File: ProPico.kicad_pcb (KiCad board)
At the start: 2 copper layers, 59 parts, among them J1 USB_C_Receptacle_USB2.0, J2 SWD, J3 LEFT, J4 RIGHT, SW1 BOOTSEL, SW2 RES, U1 FM24CL16B, U2 W25Q128JVS, U3 TLV1117-33, U4 LM4040DBZ-3, U5 RP2040, Y1 ECS-120-12-36-AGN-TR3

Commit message: started layout
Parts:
- removed C19, C20: 100n, Capacitor_SMD:C_0402_1005Metric
- removed FB1: 100 @ 100MHz, Inductor_SMD:L_0805_2012Metric_Pad1.15x1.40mm_HandSolder
- removed REF**: RPi_Pico_SMD_TH, MCU_RaspberryPi_and_Boards:RPi_Pico_SMD_TH
- C1, C5: value 2.2u -> 100n; footprint Capacitor_SMD:C_0603_1608Metric_Pad1.08x0.95mm_HandSolder -> Capacitor_SMD:C_0402_1005Metric_Pad0.74x0.62mm_HandSolder
- C10: value 100n -> 1u
- C14: value 1u -> 100n
- C2: value 100n -> 18p; footprint Capacitor_SMD:C_0402_1005Metric_Pad0.74x0.62mm_HandSolder -> Capacitor_SMD:C_0402_1005Metric
- C4: value 18p -> 2.2u; footprint Capacitor_SMD:C_0402_1005Metric -> Capacitor_SMD:C_0603_1608Metric_Pad1.08x0.95mm_HandSolder
- C6: value 2.2u -> 10u; footprint Capacitor_SMD:C_0603_1608Metric_Pad1.08x0.95mm_HandSolder -> Capacitor_SMD:C_0805_2012Metric_Pad1.18x1.45mm_HandSolder
- C7: value 100n -> 10n C0G; footprint Capacitor_SMD:C_0402_1005Metric_Pad0.74x0.62mm_HandSolder -> Capacitor_SMD:C_0603_1608Metric_Pad1.08x0.95mm_HandSolder
- C8: value 10u -> 100n; footprint Capacitor_SMD:C_0805_2012Metric_Pad1.18x1.45mm_HandSolder -> Capacitor_SMD:C_0402_1005Metric
- C9: value 10n C0G -> 100n; footprint Capacitor_SMD:C_0603_1608Metric_Pad1.08x0.95mm_HandSolder -> Capacitor_SMD:C_0402_1005Metric
- TP1: value GND -> BOOTSEL; moved to B.Cu
- TP2: value D- -> VREG; moved to B.Cu
- TP3: value D+ -> GP25; moved to B.Cu
- TP4: value GP24 -> GND
- TP5: value GP25 -> D+
- TP6: value BOOTSEL -> GP24
- TP7: value VREG -> D-
- moved D1 87.0 mm to (161.4, 54.0), turned to 90 degrees
- moved C4 78.5 mm to (160.4, 57.4), turned to 180 degrees
- moved R7 78.5 mm to (161.4, 89.6), turned to -90 degrees
- moved C11 75.6 mm to (160.5, 75.4)
- moved R10 75.3 mm to (154.1, 85.7)
- moved R5 75.2 mm to (153.2, 81.4), turned to 180 degrees
- moved R11 75.0 mm to (154.1, 86.9)
- moved C12 74.5 mm to (157.7, 68.7), turned to 90 degrees
- moved C6 73.4 mm to (161.7, 65.3), turned to -90 degrees
- moved C1 73.0 mm to (151.4, 86.9), turned to 180 degrees
- moved C14 72.8 mm to (160.5, 70.9)
- moved C10 72.6 mm to (156.7, 68.7), turned to 90 degrees
- moved R9 71.9 mm to (156.1, 66.8), turned to -90 degrees
- moved R8 71.4 mm to (155.1, 66.8), turned to -90 degrees
- moved C9 71.1 mm to (156.0, 80.6), turned to -90 degrees
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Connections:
- C1 pad 1: +5VD -> +3V3
- C11 pad 1: +1V1 -> +3V3
- C12 pad 1: +1V1 -> +3V3
- C2 pad 1: +3V3 -> /XIN
- C3 pad 1: /XIN -> Net-(C3-Pad1)
- C4 pad 1: Net-(C4-Pad1) -> +5V
- C6 pad 1: +5V -> Net-(C6-Pad1)
- C7 pad 1: +3V3 -> /ADC_AVDD
- C8 pad 1: Net-(C8-Pad1) -> +1V1
- C9 pad 1: /ADC_AVDD -> +1V1
- D1 pad 1: +5VD -> +5V
- J1 pad S1: unconnected-(J1-SHIELD-PadS1) -> GND
- R5 pad 2: Net-(C4-Pad1) -> Net-(C3-Pad1)
- R6 pad 1: Net-(C8-Pad1) -> Net-(C6-Pad1)
- TP1 pad 1: GND -> Net-(R1-Pad2)
- TP2 pad 1: /D- -> +1V1
- TP3 pad 1: /D+ -> /EEPROM_SCL
- TP4 pad 1: /EEPROM_SDA -> GND
- TP5 pad 1: /EEPROM_SCL -> /D+
- TP6 pad 1: Net-(R1-Pad2) -> /EEPROM_SDA
- TP7 pad 1: +1V1 -> /D-
- Y1 pad 1: Net-(C4-Pad1) -> Net-(C3-Pad1)
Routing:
- net Net-(J1-CC2): track 0.00 -> 2.67 mm
- net Net-(J1-CC1): track 0.00 -> 2.61 mm
- net Net-(D2-K): track 0.00 -> 1.41 mm
- net GND: vias 0 -> 4
- added copper zone on F.Cu, net +5V
- added copper zone on F.Cu, net GND
- added copper zone on F.Cu, net VBUS
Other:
- board outline added: 21 x 51 mm

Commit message: progress on layout
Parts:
- moved JP1 5.55 mm to (153.6, 95.6), turned to 0 degrees
- moved R2 5.48 mm to (150.2, 65.2)
- moved R1 4.69 mm to (147.4, 67.6), turned to 90 degrees
- moved R13 3.49 mm to (148.2, 55.8), turned to 180 degrees
- moved C2 2.74 mm to (150.1, 86.5), turned to -90 degrees
- moved C16 2.64 mm to (147.4, 69.7), turned to 90 degrees
- moved R9 2.03 mm to (157.6, 68.2)
- moved R8 2.03 mm to (156.6, 68.2)
- moved C17 2.01 mm to (147.8, 77.1)
- moved C15 1.98 mm to (154.2, 67.4), turned to 135 degrees
- moved C10 1.95 mm to (158.6, 68.2)
- moved C12 1.95 mm to (159.6, 68.2)
- moved C13 1.91 mm to (155.6, 68.7)
- moved C6 1.68 mm to (161.6, 67.0)
- moved R6 1.68 mm to (161.6, 63.1)
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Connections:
- net Net-(U5-USB_DM) renamed /DN
- net Net-(U5-USB_DP) renamed /DP
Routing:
- net /GPIO0: track 0.00 -> 26.0 mm, vias 0 -> 1
- net /GPIO1: track 0.00 -> 24.4 mm, vias 0 -> 1
- net /GPIO16: track 0.00 -> 23.8 mm, vias 0 -> 1
- net /GPIO15: track 0.00 -> 23.8 mm
- net /GPIO17: track 0.00 -> 21.7 mm, vias 0 -> 1
- net /D+: track 0.00 -> 21.6 mm, vias 0 -> 1
- net /GPIO3: track 0.00 -> 21.2 mm, vias 0 -> 2
- net /D-: track 0.00 -> 21.1 mm, vias 0 -> 1
- net /GPIO14: track 0.00 -> 21.1 mm
- net /GPIO2: track 0.00 -> 21.1 mm, vias 0 -> 2
- net +3V3: track 0.00 -> 20.2 mm, vias 0 -> 6
- net /GPIO29_ADC3: track 0.00 -> 17.5 mm, vias 0 -> 1
- net /GPIO18: track 0.00 -> 16.4 mm
- net /GPIO4: track 0.00 -> 16.4 mm, vias 0 -> 1
- net /GPIO13: track 0.00 -> 15.8 mm
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- added copper zone on F.Cu, net +1V1
- added copper zone on B.Cu, net +3V3
- added copper zone on F.Cu, net +3V3

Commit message: finished layout
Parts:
- moved C11 1.40 mm to (160.7, 77.9), turned to -90 degrees
- moved C14 0.25 mm to (161.0, 72.0)
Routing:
- net /EEPROM_SCL: track 6.52 -> 56.5 mm, vias 1 -> 4
- net +3V3: track 20.2 -> 65.5 mm, vias 6 -> 5
- net /EEPROM_SDA: track 7.35 -> 48.5 mm, vias 1 -> 2
- net /GPIO23: track 3.68 -> 31.6 mm, vias 1 -> 2
- net /RUN: track 6.77 -> 34.6 mm, vias 1 -> 3
- net /ADC_AVDD: track 4.09 -> 28.8 mm, vias 1 -> 2
- net /SWCLK: track 6.79 -> 22.7 mm
- net /SWD: track 6.53 -> 21.0 mm
- net Net-(R1-Pad2): track 0.00 -> 12.7 mm, vias 0 -> 1
- net +1V1: track 6.60 -> 11.8 mm, vias 0 -> 1
- net /3V0_VREF: track 0.00 -> 4.71 mm
- net Net-(D3-K): track 0.00 -> 1.91 mm
- net GND: track 8.69 -> 9.35 mm, vias 10 -> 30
- net /QSPI_SCLK: track 7.71 -> 7.16 mm
- net /QSPI_SD3: track 8.94 -> 8.40 mm
- added copper zone on B.Cu, net GND

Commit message: finished erc
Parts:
- moved C3 0.13 mm to (154.1, 83.3)

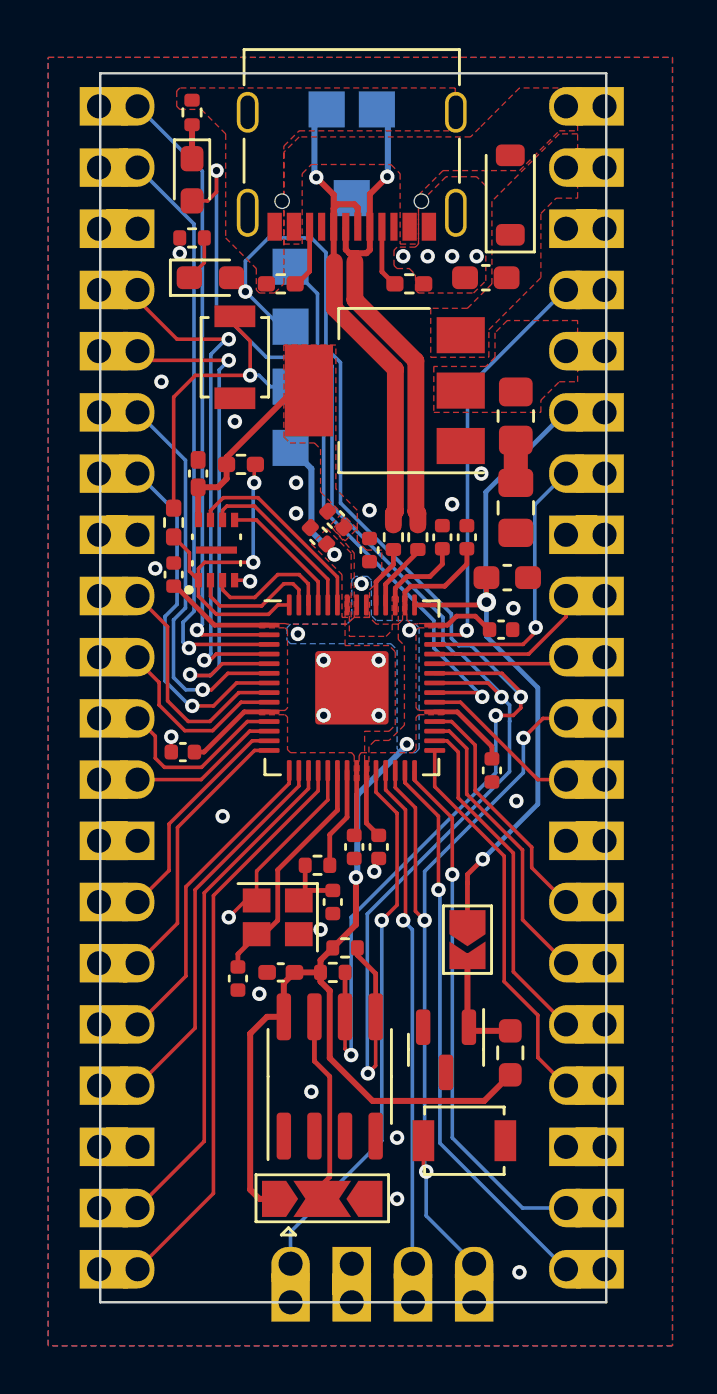
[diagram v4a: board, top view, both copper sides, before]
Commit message: finished silkscreen
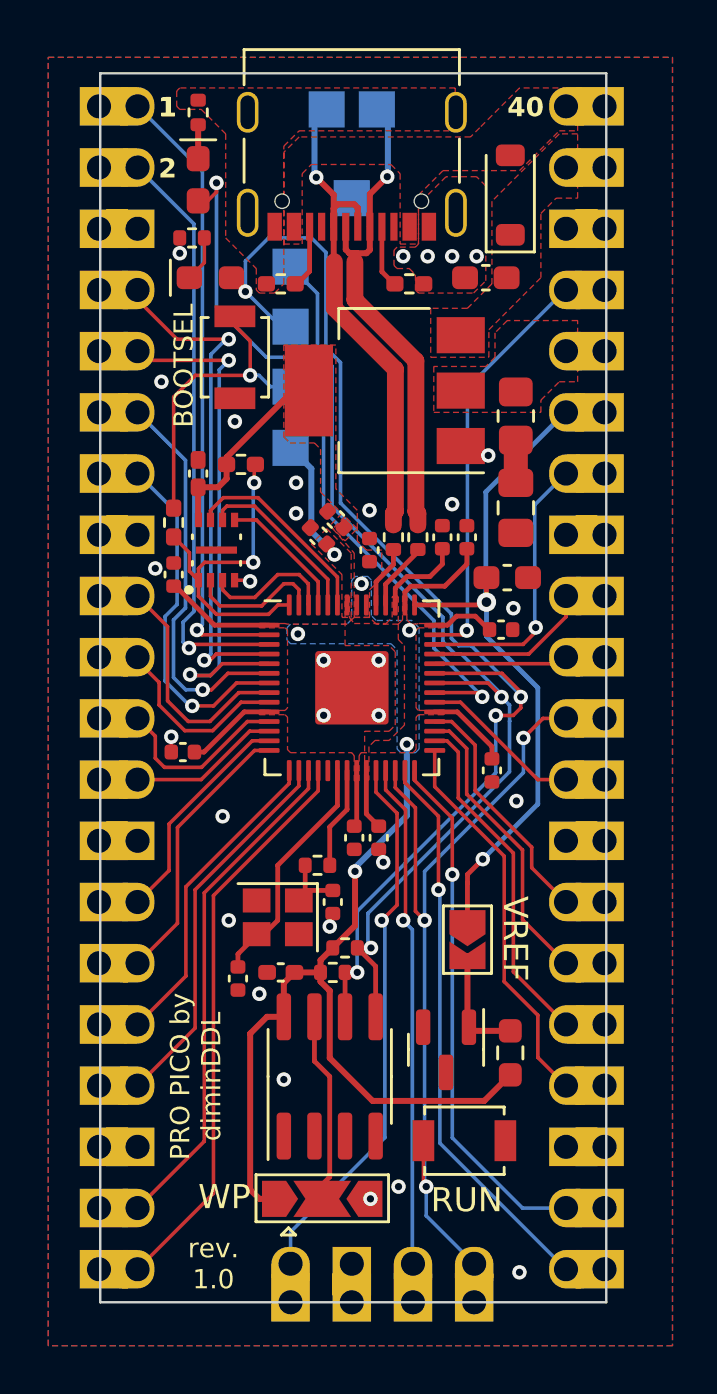
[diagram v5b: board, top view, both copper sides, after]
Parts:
- added G***: LOGO, LOGO, B.Cu at (154.9, 90.6)
- moved C18 0.38 mm to (154.9, 80.6)
- moved C9 0.38 mm to (156.0, 80.6)
- moved D2 0.25 mm to (148.5, 53.3)
- moved R12 0.25 mm to (148.5, 50.5)
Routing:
- net GND: track 9.35 -> 1.30 mm
- net /EEPROM_SDA: track 48.5 -> 41.4 mm
- net /EEPROM_SCL: track 56.5 -> 51.8 mm
- net /GPIO23: track 31.6 -> 30.3 mm
- net /RUN: track 34.6 -> 35.2 mm
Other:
- board text added: "1"
- board text added: "1V1"
- board text added: "2"
- board text added: "3V3"
- board text added: "40"
- board text added: "ADC_VERF"
- board text added: "BOOTSEL"
- board text added: "CLK"
- board text added: "D+"
- board text added: "D-"
- board text added: "FLASH"
- board text added: "GND"
- board text added: "GP0"
- board text added: "GP1"
- board text added: "GP10"
- board text added: "GP11"
- board text added: "GP12"
- board text added: "GP13"
- board text added: "GP14"
- board text added: "GP15"
- board text added: "GP16"
- board text added: "GP17"
- board text added: "GP18"
- board text added: "GP19"
- board text added: "GP2"
- board text added: "GP20"
- board text added: "GP21"
- board text added: "GP22"
- board text added: "GP24"
- board text added: "GP25"
- board text added: "GP26_ADC0"
- board text added: "GP27_ADC1"
- board text added: "GP28_ADC2"
- board text added: "GP29_ADC3"
- board text added: "GP3"
- board text added: "GP4"
- board text added: "GP5"
- board text added: "GP6"
- board text added: "GP7"
- board text added: "GP8"
- board text added: "GP9"
- board text added: "PRO PICO by diminDDL"
- board text added: "RUN"
- board text added: "SIO"
- board text added: "VBUS"
- board text added: "VREF"
- board text added: "VSYS"
- board text added: "WP"
- board text added: "rev. 1.0"
- board text added: "■ ■ 2MB ■ □ 4MB □ ■ 8MB □ □ 16MB"

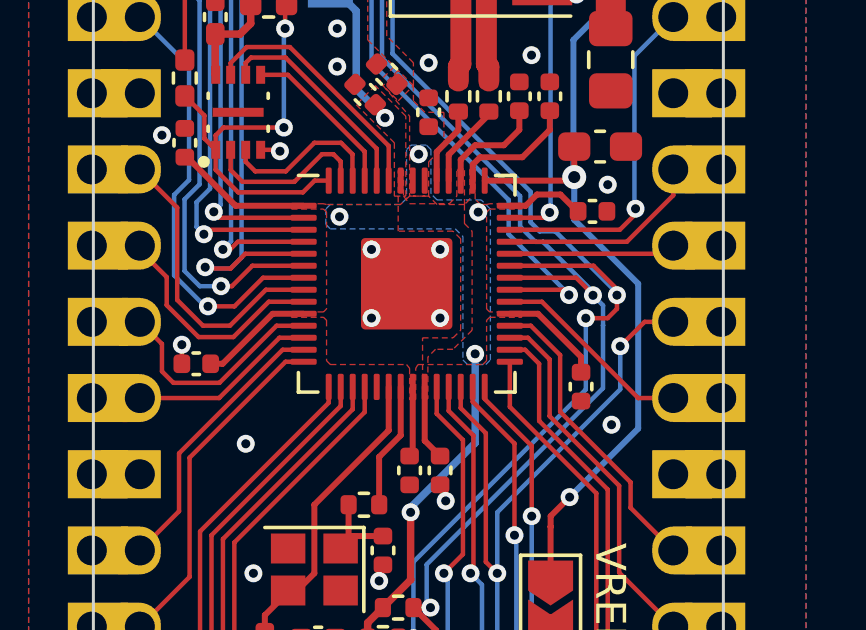
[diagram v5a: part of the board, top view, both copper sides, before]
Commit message: added render, fixed spelling mistake
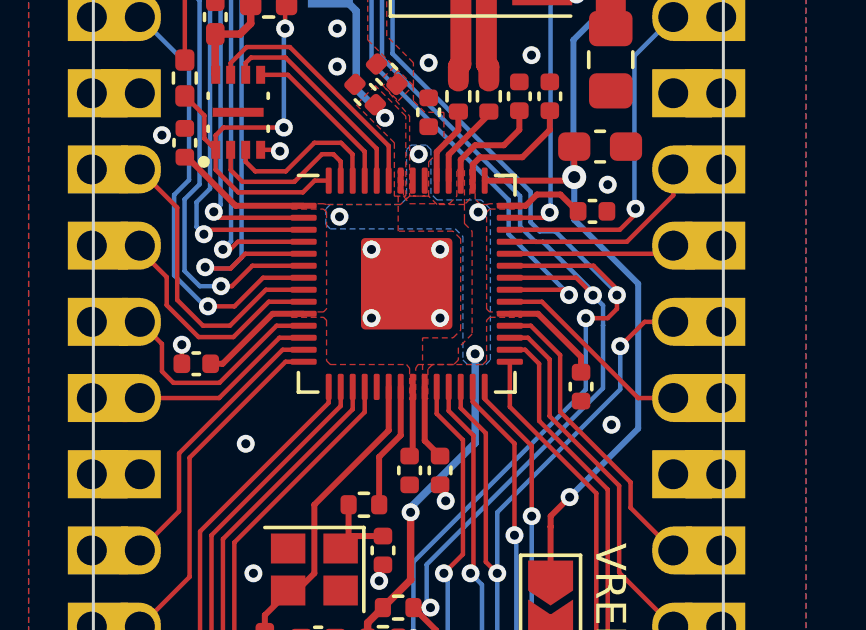
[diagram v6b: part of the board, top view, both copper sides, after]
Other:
- board text added: "ADC_VREF"
- board text added: "PCB3D_BR_propico"
- board text added: "PCB3D_TL_propico"
- board text removed: "ADC_VERF"
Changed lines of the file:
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@@
     (effects (font (size 0.8 0.8) (thickness 0.15)) (justify left bottom mirror))
   )
-  (gr_text "ADC_VERF" (at 162.433 63.5) (layer "B.SilkS")
+  (gr_text "ADC_VREF" (at 162.433 63.5) (layer "B.SilkS")
     (effects (font (size 0.8 0.8) (thickness 0.15)) (justify left bottom mirror))
   )
@@
   )
   (gr_text "VREF" (at 161.036 83.058 -90) (layer "F.SilkS")
+    (effects (font (size 1 1) (thickness 0.15)) (justify left bottom))
+  )
+  (gr_text "PCB3D_TL_propico" (at 126.0348 43.942) (layer "Eco1.User")
+    (effects (font (size 1 1) (thickness 0.15)) (justify left bottom))
+  )
+  (gr_text "PCB3D_BR_propico" (at 174.5488 104.2416) (layer "Eco1.User")
     (effects (font (size 1 1) (thickness 0.15)) (justify left bottom))
   )
@@
         (xy 156.7688 72.4154)
         (xy 157.0228 72.6694)
-        (xy 157.0228 75.9714)
-        (xy 156.3878 76.6064)
-        (xy 155.8036 76.6064)
-        (xy 155.5496 76.8604)
+        (xy 157.0228 76.0984)
+        (xy 156.5656 76.5556)
+        (xy 156.5656 76.962)
+        (xy 156.4132 77.1144)
+        (xy 155.702 77.1144)
+        (xy 155.5496 77.2668)
         (xy 155.5496 78.2574)
       )

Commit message: made schematic less cringe
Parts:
- moved C4 52.8 mm to (108.4, 47.8)
- moved C8 52.8 mm to (101.5, 58.5)
- moved JP2 52.8 mm to (107.7, 75.3)
- moved R2 52.8 mm to (98.3, 55.5)
- moved C1 52.8 mm to (99.9, 76.6)
- moved C10 52.8 mm to (106.6, 58.6)
- moved C11 52.8 mm to (108.7, 68.2)
- moved C14 52.8 mm to (109.1, 62.4)
- moved C15 52.8 mm to (102.2, 57.8)
- moved C16 52.8 mm to (95.5, 60.1)
- moved C17 52.8 mm to (95.9, 67.5)
- moved C18 52.8 mm to (103.0, 71.0)
- moved C2 52.8 mm to (98.1, 76.9)
- moved C6 52.8 mm to (109.7, 57.4)
- moved D1 52.8 mm to (109.4, 44.4)
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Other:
- board text removed: "TODO: check EEPROM pinouts check diode footprint and pins"

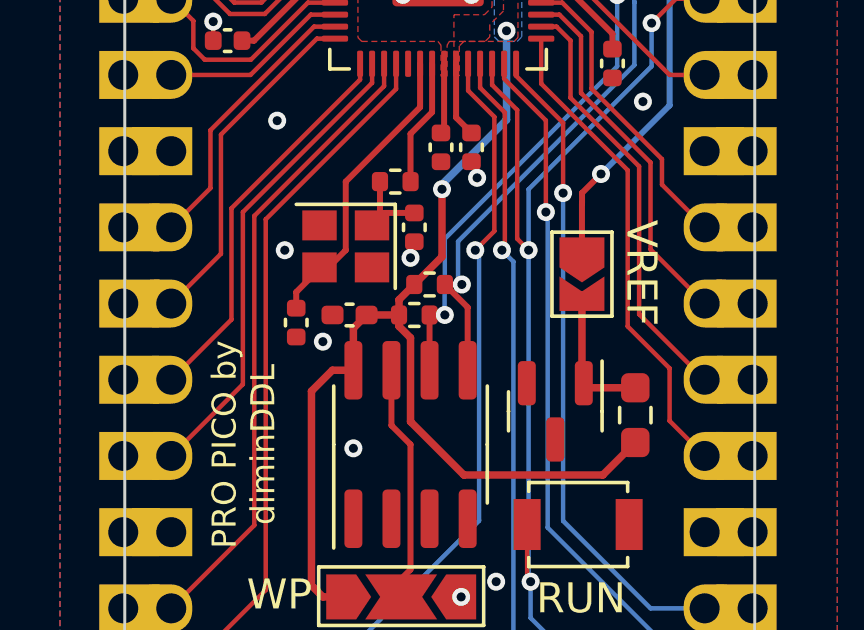
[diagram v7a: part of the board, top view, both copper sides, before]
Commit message: changed the names of some nets to be more logical
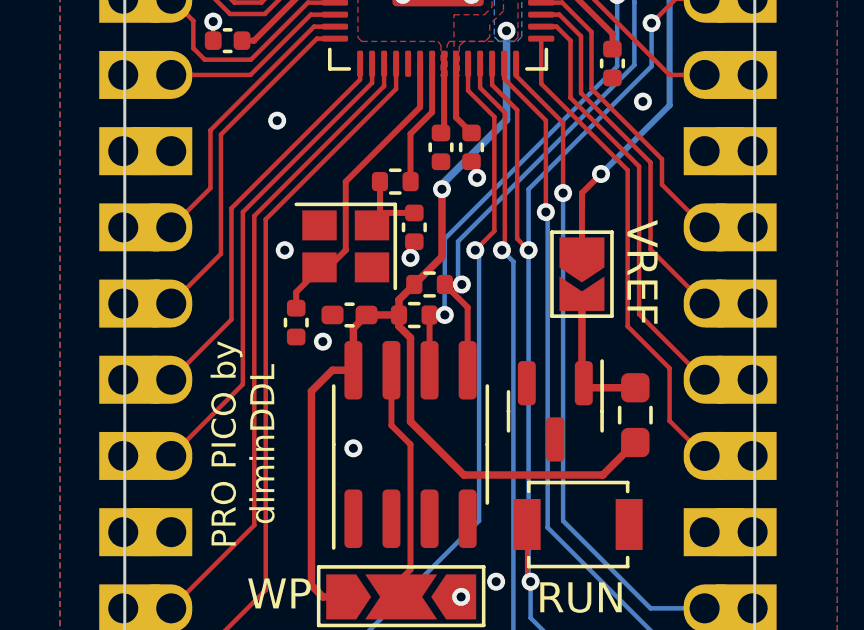
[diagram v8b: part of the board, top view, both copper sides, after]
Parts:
- R10, R11: value 4.7k -> 1k
- R2: value 10k -> DNP
- R6: value 5R -> 470mOhm
- U2: value W25Q128JVS -> W25Q16JVUXIQ
- U3: value TLV1117-33 -> AMS1117-3.3
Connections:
- net /ADC_AVDD renamed /ADC_VREF
